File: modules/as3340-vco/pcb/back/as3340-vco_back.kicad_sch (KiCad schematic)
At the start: 34 parts, among them U2 L79L05_TO92

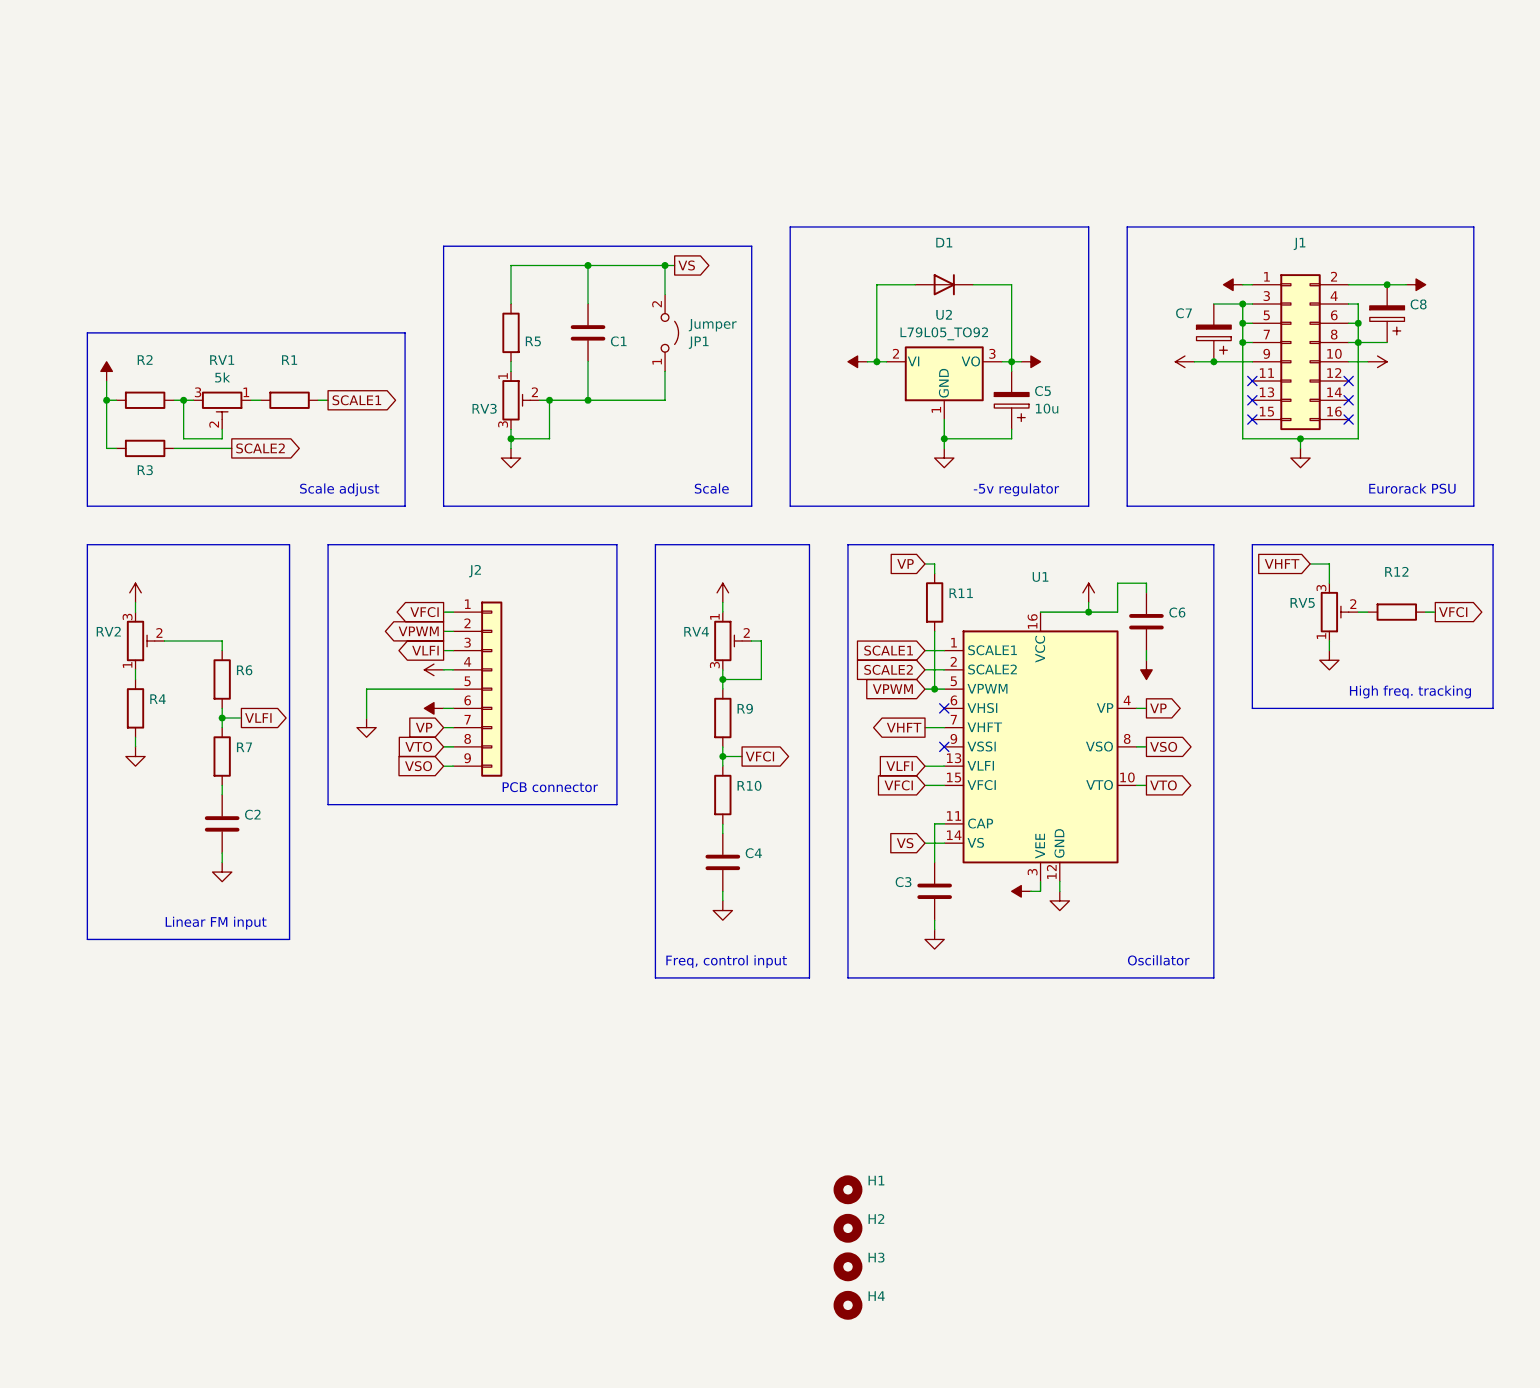
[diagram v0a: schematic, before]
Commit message: modules: as3340-vco: back: revision A (redesign)
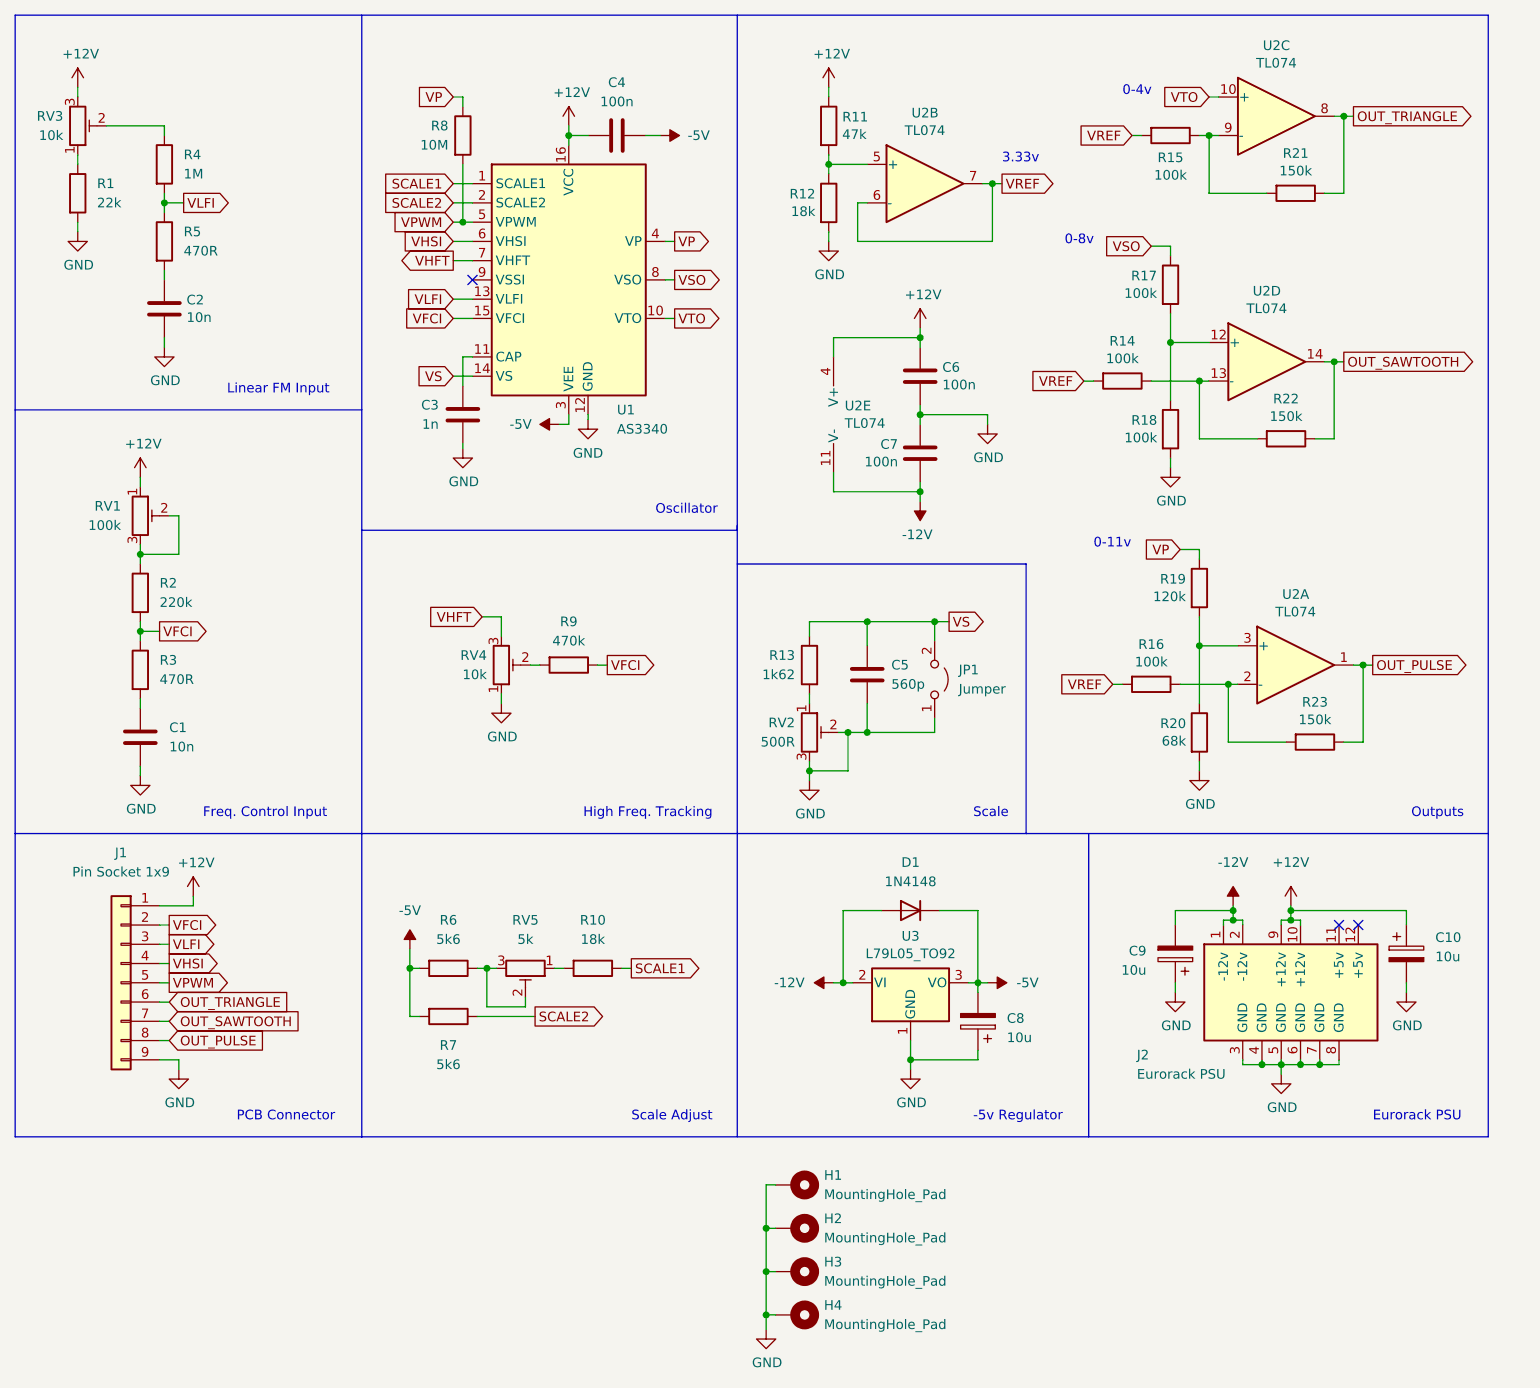
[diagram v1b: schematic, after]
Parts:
- removed C5: 10u, Capacitor_THT:CP_Radial_D5.0mm_P2.50mm, symbol Device:C_Polarized
- removed C7: (no value), symbol Device:C_Polarized
- removed H1, H2, H3, H4: (no value), symbol Mechanical:MountingHole
- removed J1: (no value), symbol Connector_Generic:Conn_02x08_Odd_Even
- removed J2: (no value), symbol Connector_Generic:Conn_01x09
- removed U2: L79L05_TO92, Package_TO_SOT_THT:TO-92_Wide, symbol Regulator_Linear:L79L05_TO92
- added C10, C9: 10u, Capacitor_THT:CP_Radial_D5.0mm_P2.50mm, symbol Device:C_Polarized
- added C5: 560p, Capacitor_THT:C_Disc_D3.0mm_W1.6mm_P2.50mm, symbol Device:C
- added C7: 100n, Capacitor_THT:C_Disc_D4.7mm_W2.5mm_P5.00mm, symbol Device:C
- added H1, H2, H3, H4: MountingHole_Pad, MountingHole:MountingHole_2.2mm_M2_Pad_Via, symbol Mechanical:MountingHole_Pad
- added J1: Pin Socket 1x9, Connector_PinSocket_2.54mm:PinSocket_1x09_P2.54mm_Vertical, symbol Connector_Generic:Conn_01x09
- added J2: Eurorack PSU, eurorack:IDC-Header_2x08_P2.54mm_Vertical, symbol eurorack:Connector_Eurorack_PSU
- added R13: 1k62, Resistor_THT:R_Axial_DIN0207_L6.3mm_D2.5mm_P10.16mm_Horizontal, symbol Device:R
- added R14, R15, R16, R17, R18: 100k, Resistor_THT:R_Axial_DIN0207_L6.3mm_D2.5mm_P10.16mm_Horizontal, symbol Device:R
- added R19: 120k, Resistor_THT:R_Axial_DIN0207_L6.3mm_D2.5mm_P10.16mm_Horizontal, symbol Device:R
- added R20: 68k, Resistor_THT:R_Axial_DIN0207_L6.3mm_D2.5mm_P10.16mm_Horizontal, symbol Device:R
- added R21, R22, R23: 150k, Resistor_THT:R_Axial_DIN0207_L6.3mm_D2.5mm_P10.16mm_Horizontal, symbol Device:R
- added R8: 10M, Resistor_THT:R_Axial_DIN0207_L6.3mm_D2.5mm_P10.16mm_Horizontal, symbol Device:R
- added U2: TL074, Package_DIP:DIP-14_W7.62mm, symbol Amplifier_Operational:TL074
- added U3: L79L05_TO92, Package_TO_SOT_THT:TO-92_Wide, symbol Regulator_Linear:L79L05_TO92
- C1, C2: value (none) -> 10n; footprint (none) -> Capacitor_THT:C_Disc_D3.0mm_W1.6mm_P2.50mm
- C3: value (none) -> 1n; footprint (none) -> Capacitor_THT:C_Rect_L7.2mm_W3.0mm_P5.00mm_FKS2_FKP2_MKS2_MKP2
- C4, C6: value (none) -> 100n; footprint (none) -> Capacitor_THT:C_Disc_D4.7mm_W2.5mm_P5.00mm
- C8: value (none) -> 10u; footprint (none) -> Capacitor_THT:CP_Radial_D5.0mm_P2.50mm
- D1: value (none) -> 1N4148; footprint (none) -> Diode_THT:D_DO-35_SOD27_P7.62mm_Horizontal
- R1: value (none) -> 22k; footprint (none) -> Resistor_THT:R_Axial_DIN0207_L6.3mm_D2.5mm_P10.16mm_Horizontal
- R10, R12: value (none) -> 18k; footprint (none) -> Resistor_THT:R_Axial_DIN0207_L6.3mm_D2.5mm_P10.16mm_Horizontal
- R11: value (none) -> 47k; footprint (none) -> Resistor_THT:R_Axial_DIN0207_L6.3mm_D2.5mm_P10.16mm_Horizontal
- R2: value (none) -> 220k; footprint (none) -> Resistor_THT:R_Axial_DIN0207_L6.3mm_D2.5mm_P10.16mm_Horizontal
- R3, R5: value (none) -> 470R; footprint (none) -> Resistor_THT:R_Axial_DIN0207_L6.3mm_D2.5mm_P10.16mm_Horizontal
- R4: value (none) -> 1M; footprint (none) -> Resistor_THT:R_Axial_DIN0207_L6.3mm_D2.5mm_P10.16mm_Horizontal
- R6, R7: value (none) -> 5k6; footprint (none) -> Resistor_THT:R_Axial_DIN0207_L6.3mm_D2.5mm_P10.16mm_Horizontal
- R9: value (none) -> 470k; footprint (none) -> Resistor_THT:R_Axial_DIN0207_L6.3mm_D2.5mm_P10.16mm_Horizontal
- RV1: value 5k -> 100k
- RV2: value (none) -> 500R; footprint (none) -> eurorack:Potentiometer_Vishay_M64Y_Horizontal
- RV3, RV4: value (none) -> 10k; footprint (none) -> eurorack:Potentiometer_Vishay_M64Y_Horizontal
- RV5: value (none) -> 5k; footprint (none) -> eurorack:Potentiometer_Vishay_M64Y_Horizontal
- U1: value (none) -> AS3340; footprint (none) -> Package_DIP:DIP-16_W7.62mm
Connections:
- net +12V: now also C4.1, R11.1, RV1.1, RV3.3, C10.1, J1.1 (Pin_1), J2.10 (+12v), J2.9 (+12v), U2.4 (V+); no longer RV2.3, RV4.1
- net -12V: now also C7.2, C9.2, J2.1 (-12v), J2.2 (-12v), U2.11 (V-), U3.2 (VI); no longer C8.2
- net -5V: now also C4.2, C8.2, R6.2, R7.2, U3.3 (VO); no longer C6.2, R2.2, R3.2
- net GND: now also C6.2, R1.2, R12.2, RV2.2, RV2.3, RV4.1, C10.2, C5.2, C7.1, C9.1, H1.1, H2.1, H3.1, H4.1, J1.9 (Pin_9), J2.3 (GND), J2.4 (GND), J2.5 (GND), J2.6 (GND), J2.7 (GND), J2.8 (GND), R18.2, R20.2, U3.1 (GND); no longer C4.2, R4.2, RV3.2, RV3.3, RV5.1
- net SCALE1: now also R10.1; no longer R1.1
- net SCALE2: now also R7.1; no longer R3.1
- net VFCI: now also R2.2, R3.1, R9.1, J1.2 (Pin_2); no longer R10.1, R12.1, R9.2
- net VHFT: now also RV4.3; no longer RV5.3
- net VLFI: now also R4.2, R5.1, J1.3 (Pin_3); no longer R6.2, R7.1
- net VP: now also R19.1, R8.1; no longer R11.1
- net VPWM: now also J1.5 (Pin_5), R8.2; no longer R11.2
- net VS: now also C5.1, R13.1; no longer C1.1, R5.1
- net VSO: now also R17.1
- net VTO: now also U2.10 (+)
- net VHSI: now reaches U1.6 (VHSI)
- net VHSI: now also J1.4 (Pin_4)
- net at RV2.1: now also R13.2; no longer R4.1
- net at R6.1: now also RV5.2, RV5.3; no longer RV2.2
- net at R5.2: now also C2.1; no longer RV3.1
- net at R10.2: now also RV5.1; no longer C4.1
- new net: R11.2, R12.1, U2.5 (+)
- new net: R17.2, R18.1, U2.12 (+)
- new net: R19.2, R20.1, U2.3 (+)
- new net: R16.1, R23.2, U2.2 (-)
- new net: R15.1, R21.2, U2.9 (-)
- new net: R14.1, R22.2, U2.13 (-)
- new net: R9.2, RV4.2
- new net: R1.1, RV3.1
- new net: R4.1, RV3.2
- new net: C1.1, R3.2
- new net OUT_PULSE: J1.8 (Pin_8), R23.1, U2.1
- new net OUT_SAWTOOTH: J1.7 (Pin_7), R22.1, U2.14
- new net OUT_TRIANGLE: J1.6 (Pin_6), R21.1, U2.8
- new net VREF: R14.2, R15.2, R16.2, U2.6 (-), U2.7
- no-connect marks 8 -> 3
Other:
- note added: "-5v Regulator"
- note added: "0-11v"
- note added: "0-4v"
- note added: "0-8v"
- note added: "3.33v"
- note added: "Freq. Control Input"
- note added: "High Freq. Tracking"
- note added: "Linear FM Input"
- note added: "Outputs"
- note added: "PCB Connector"
- note added: "Scale Adjust"
- note removed: "-5v regulator"
- note removed: "Freq, control input"
- note removed: "High freq. tracking"
- note removed: "Linear FM input"
- note removed: "PCB connector"
- note removed: "Scale adjust"
- company: (none) -> eurorack.rgm.io
